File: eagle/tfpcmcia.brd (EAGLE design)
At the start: 80.4 x 44.4 mm, 13 parts, among them IC1 CH32V307, IC2 LM1117MPX-3.3, IC3 APS6404L-3SQR-SN, J2 MSD-11-A

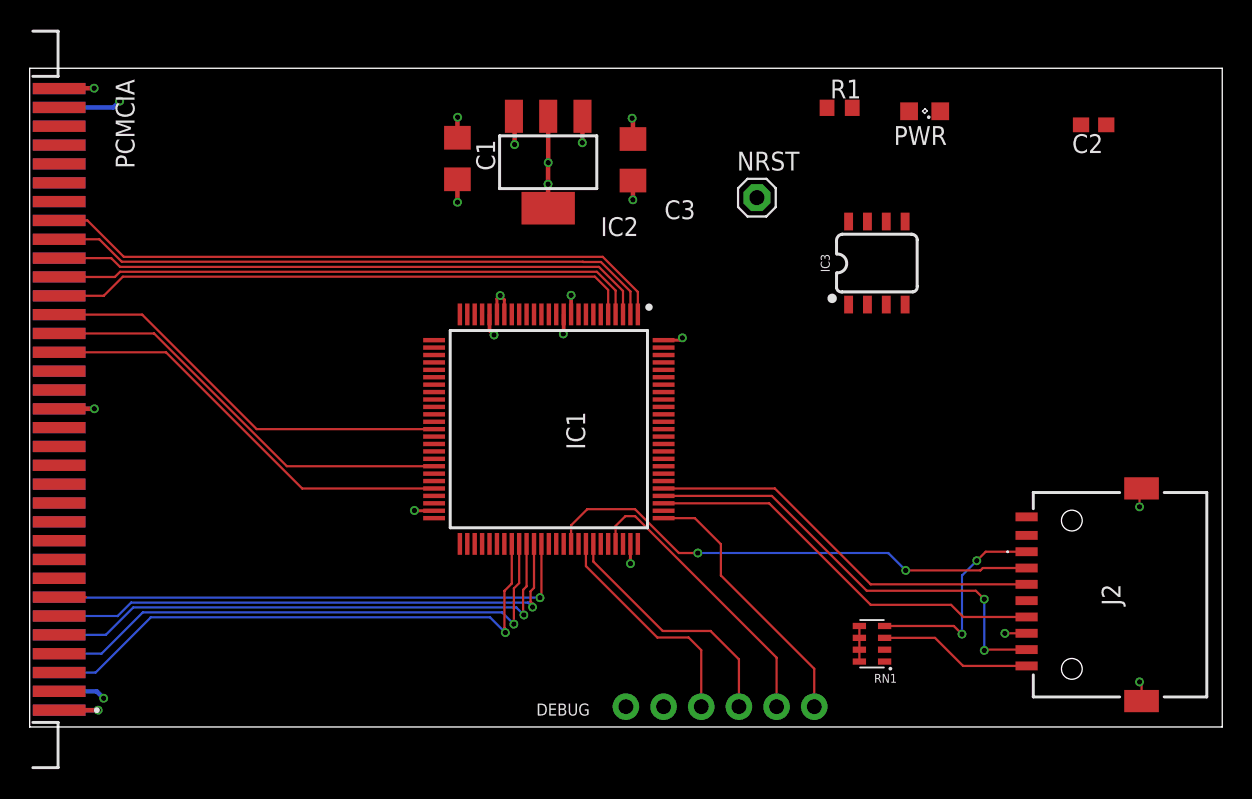
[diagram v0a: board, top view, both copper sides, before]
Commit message: Finished routing, unchecked schematic
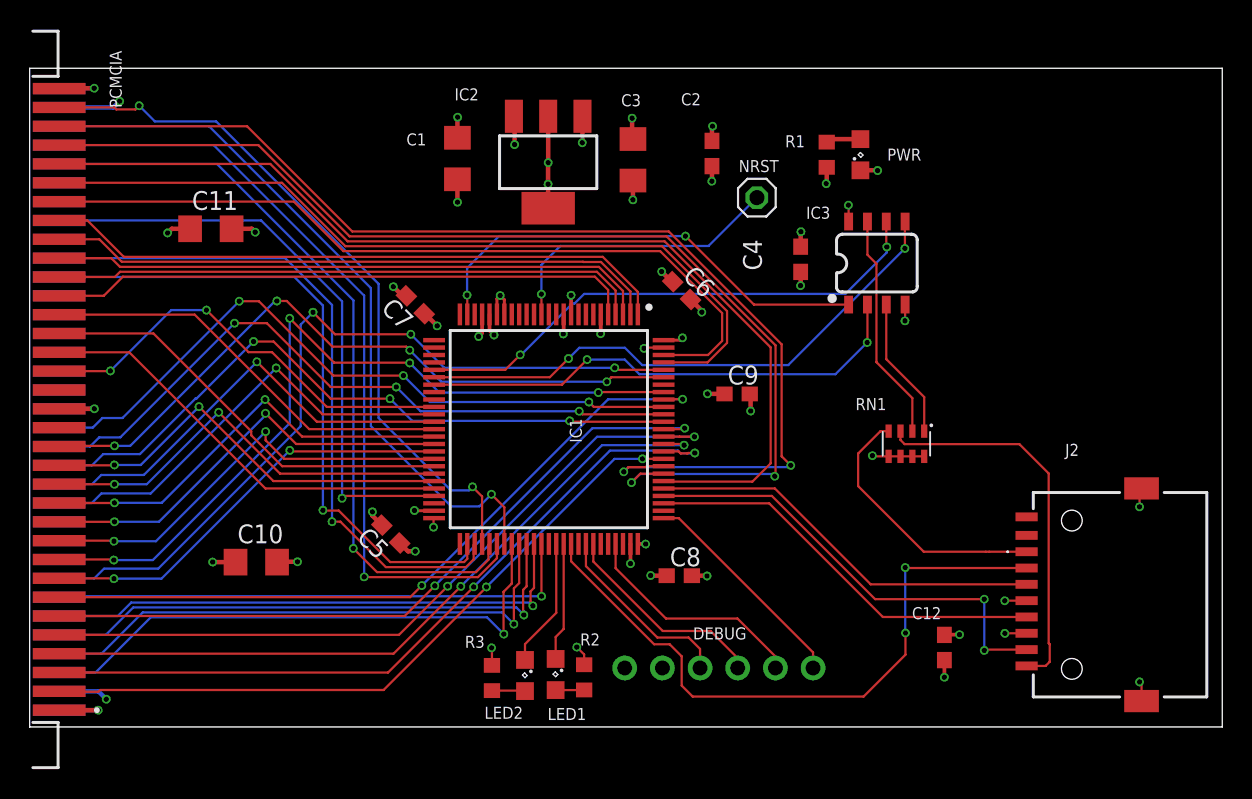
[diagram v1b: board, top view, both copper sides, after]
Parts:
- added C10, C11: 22uF, rcl:C1206
- added C12, C4, C5, C6, C7, C8, C9: 100nF, eagle-ltspice:C0603
- added LED1, LED2: LED, led:SML0805
- added R2, R3: 2K2, rcl:R0603
- moved C2 25.8 mm to (46.0, 38.7), turned to 270 degrees
- moved RN1 13.7 mm to (59.1, 19.1), turned to 270 degrees
- moved PWR 5.23 mm to (56.0, 38.6), turned to 90 degrees
- moved R1 3.28 mm to (53.7, 38.6), turned to 90 degrees
- moved DEBUG 2.61 mm to (46.5, 3.98)
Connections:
- new net LED1: IC1.65, LED1.C
- new net LED2: IC1.64, LED2.C
- new net N$5: LED1.A, R2.2
- new net N$6: LED2.A, R3.2
- net GND: now also C10.2, C11.2, C12.2, C4.2, C5.2, C6.2, C7.2, C8.2, C9.2
- net VCC: now also C10.1, C11.1
- net VCC33: now also C12.1, C4.1, C5.1, C6.1, C7.1, C8.1, C9.1, R2.1, R3.1
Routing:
- net D2: track 0.00 -> 77.5 mm, vias 0 -> 2
- net D1: track 0.00 -> 75.1 mm, vias 0 -> 2
- net D0: track 0.26 -> 68.7 mm
- net A0: track 0.00 -> 55.6 mm
- net A1: track 0.00 -> 54.0 mm
- net D9: track 0.16 -> 54.2 mm, vias 0 -> 1
- net CE2: track 0.00 -> 53.8 mm, vias 0 -> 3
- net OE: track 0.00 -> 53.8 mm, vias 0 -> 4
- net D8: track 0.00 -> 51.6 mm, vias 0 -> 1
- net D4: track 0.00 -> 51.3 mm, vias 0 -> 2
- net D6: track 0.00 -> 50.4 mm, vias 0 -> 2
- net D5: track 0.00 -> 49.4 mm, vias 0 -> 2
- net D10: track 0.00 -> 49.3 mm, vias 0 -> 1
- net D7: track 0.00 -> 48.9 mm, vias 0 -> 2
- net WP/!IOCS16: track 0.00 -> 48.3 mm, vias 0 -> 2
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- added copper zone on layer 2, net VCC33

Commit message: updated the audio section
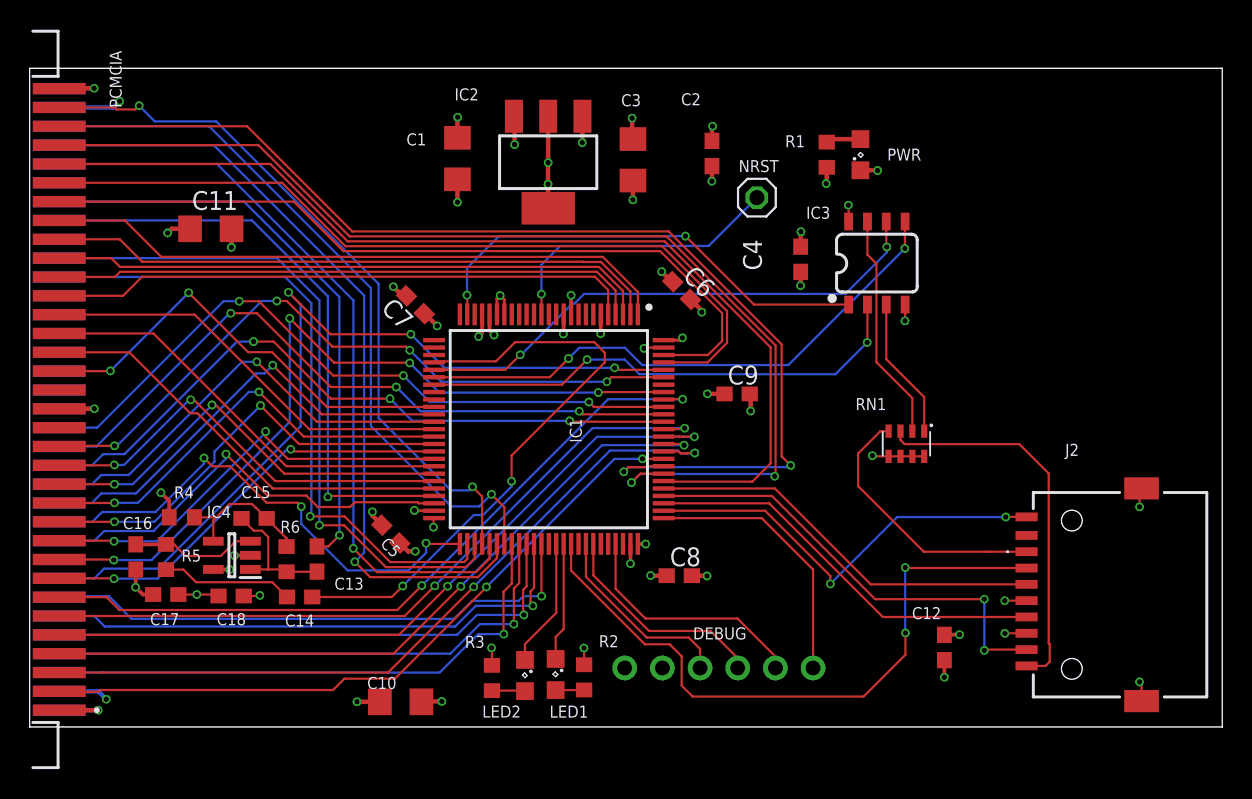
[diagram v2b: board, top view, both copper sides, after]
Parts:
- added C13, C14: 4.7uF, eagle-ltspice:C0603
- added C15, C16: 1nF, eagle-ltspice:C0603
- added C17: 1uF, eagle-ltspice:C0603
- added C18: 100nF, eagle-ltspice:C0603
- added IC4: MCP6001RT-I_OT, SamacSys_Parts:SOT95P270X145-5N
- added R4, R5, R6: 10k, rcl:R0603
- moved C10 13.5 mm to (25.0, 1.70)
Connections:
- removed net BVD2: PCMCIA.62
- removed net CD: J2.P9
- new net AUD_MIXED: C14.1, IC1.29
- new net AUD_O: C13.1, PCMCIA.62
- new net N$10: C15.1, IC4.4, R4.2, R6.1
- new net N$7: C13.2, C15.2, IC4.1, R6.2
- new net N$8: C16.1, IC4.3, R5.1
- new net N$9: C14.2, R5.2
- new net SD_CD: IC1.77, J2.P9
- net GND: now also C16.2, C17.2, C18.2, IC4.5, R4.1
- net IORD: now also IC1.48
- net IOWR: now also IC1.51
- net VCC: now also C17.1, C18.1, IC4.2
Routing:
- net AUD_MIXED: track 0.00 -> 40.5 mm, vias 0 -> 2
- net AUD_O: track 0.00 -> 39.4 mm, vias 0 -> 1
- net IOWR: track 0.00 -> 34.0 mm, vias 0 -> 3
- net IORD: track 0.00 -> 29.5 mm, vias 0 -> 1
- net SD_CD: track 0.00 -> 28.7 mm, vias 0 -> 2
- net N$10: track 0.00 -> 9.80 mm
- net N$7: track 0.00 -> 9.07 mm
- net N$9: track 0.00 -> 8.93 mm
- net N$8: track 0.00 -> 8.47 mm
- net GND: track 48.7 -> 55.0 mm, vias 27 -> 31
- net VCC: track 12.2 -> 16.1 mm, vias 6 -> 8
- net CE2: track 53.8 -> 57.4 mm
- net SWCLK: track 14.9 -> 18.2 mm
- net D15: track 36.1 -> 37.3 mm
- net A16: track 29.7 -> 30.7 mm
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
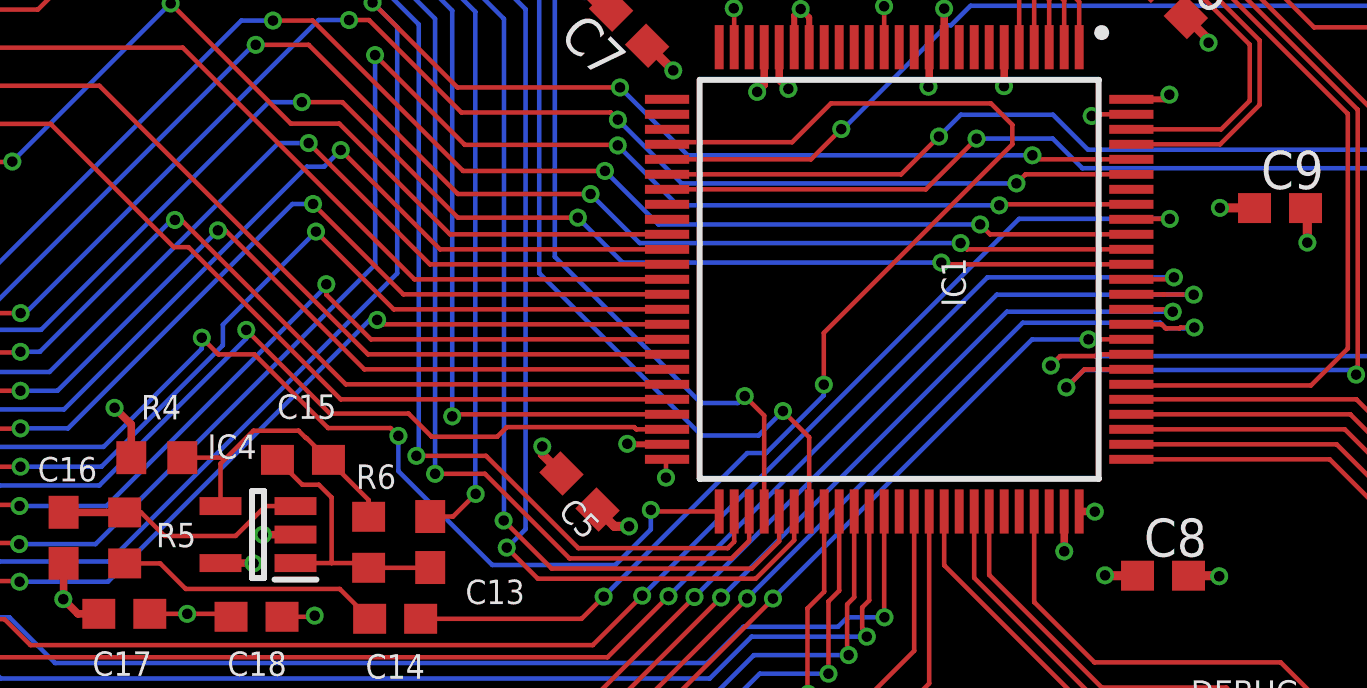
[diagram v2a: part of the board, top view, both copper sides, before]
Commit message: fixed BOOT0
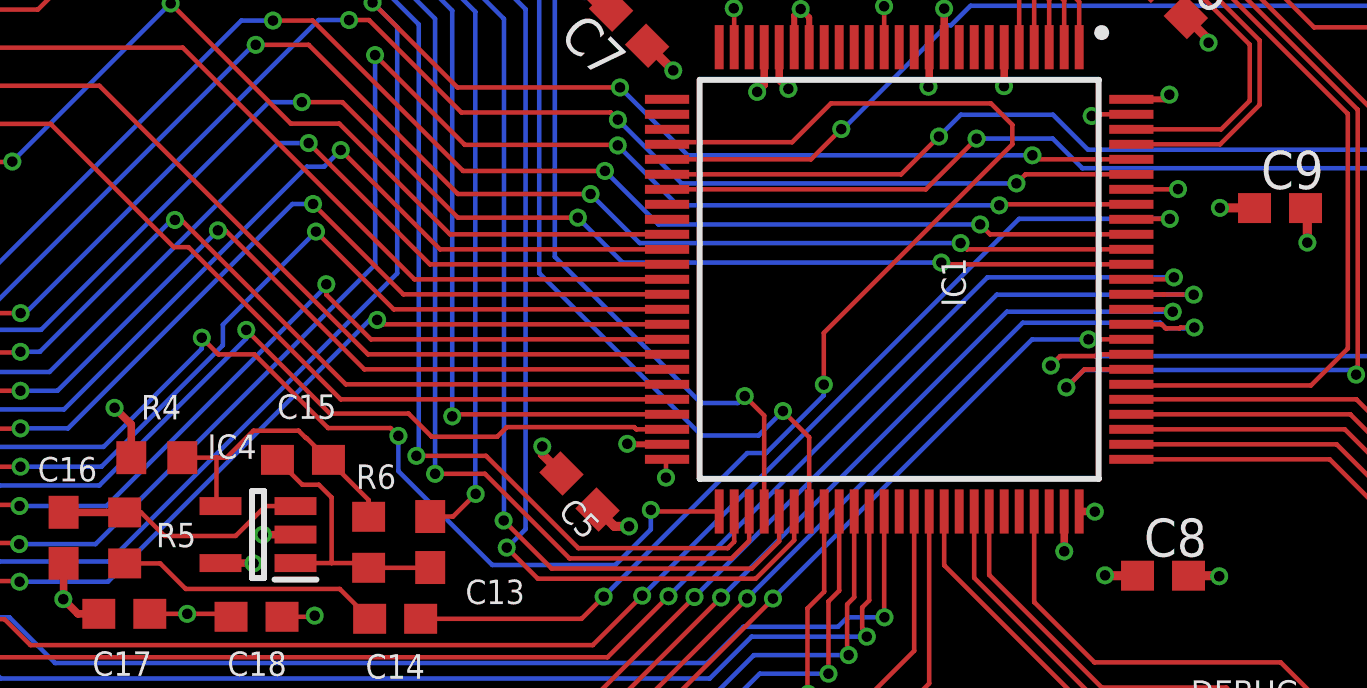
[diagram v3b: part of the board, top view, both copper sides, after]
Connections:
- net GND: now also IC1.94
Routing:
- net GND: track 55.0 -> 56.5 mm, vias 31 -> 32
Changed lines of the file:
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@@
 <wire x1="12.3825875" y1="10.62205" x2="13.475225" y2="10.62205" width="0.254" layer="1"/>
 <wire x1="13.475225" y1="10.62205" x2="13.484315625" y2="10.612959375" width="0.254" layer="1"/>
+<contactref element="IC1" pad="94"/>
+<wire x1="42.743509375" y1="23.08000625" x2="44.290403125" y2="23.08000625" width="0.1524" layer="1"/>
+<wire x1="44.290403125" y1="23.08000625" x2="44.29944375" y2="23.089046875" width="0.1524" layer="1"/>
+<via x="44.29944375" y="23.089046875" extent="1-16" drill="0.35"/>
 </signal>
 <signal name="D3">
@@
 <via x="41.5271625" y="12.3359375" extent="1-16" drill="0.35"/>
 <polygon width="0.1524" layer="2" isolate="0.3048">
-<vertex x="25.85433125" y="38.5838125"/>
+<vertex x="25.241496875" y="38.5838125"/>
 <vertex x="35.76589375" y="38.5838125"/>
 <vertex x="35.78806875" y="38.6059875"/>
@@
 <vertex x="22.0744" y="11.939046875"/>
 <vertex x="22.0744" y="35.416715625"/>
-<vertex x="25.674971875" y="39.0172875"/>
 </polygon>
 <via x="30.2715375" y="26.32878125" extent="1-16" drill="0.35"/>
@@
 <wire x1="15.98069375" y1="14.061640625" x2="17.320125" y2="12.722209375" width="0.1524" layer="1"/>
 <wire x1="17.320125" y1="12.722209375" x2="17.320125" y2="12.164615625" width="0.1524" layer="1"/>
-<wire x1="12.3825875" y1="12.52205" x2="12.3825875" y2="13.934775" width="0.1524" layer="1"/>
-<wire x1="12.58389375" y1="14.13608125" x2="12.3825875" y2="13.934775" width="0.1524" layer="1"/>
 <wire x1="15.98069375" y1="14.061640625" x2="15.250065625" y2="14.79226875" width="0.1524" layer="1"/>
 <wire x1="15.250065625" y1="14.79226875" x2="15.22719375" y2="14.79226875" width="0.1524" layer="1"/>
 <wire x1="15.22719375" y1="14.79226875" x2="14.985571875" y2="15.033890625" width="0.1524" layer="1"/>
-<wire x1="14.985571875" y1="15.033890625" x2="13.481703125" y2="15.033890625" width="0.1524" layer="1"/>
-<wire x1="11.108565625" y1="14.13608125" x2="12.58389375" y2="14.13608125" width="0.1524" layer="1"/>
+<wire x1="13.481703125" y1="15.033890625" x2="14.985571875" y2="15.033890625" width="0.1524" layer="1"/>
+<wire x1="11.108565625" y1="14.13608125" x2="12.24835625" y2="14.13608125" width="0.1524" layer="1"/>
+<wire x1="12.24835625" y1="14.13608125" x2="12.58389375" y2="14.13608125" width="0.1524" layer="1"/>
 <wire x1="12.58389375" y1="14.13608125" x2="13.481703125" y2="15.033890625" width="0.1524" layer="1"/>
+<wire x1="12.3825875" y1="12.52205" x2="12.24835625" y2="12.65628125" width="0.1524" layer="1"/>
+<wire x1="12.24835625" y1="12.65628125" x2="12.24835625" y2="14.13608125" width="0.1524" layer="1"/>
 </signal>
 </signals>
